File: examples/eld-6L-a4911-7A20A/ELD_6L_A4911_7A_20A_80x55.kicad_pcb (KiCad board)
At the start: 6 copper layers, 80 x 55 mm, 103 parts, among them J1 BAT/IGN/GND, J2 DAP, J3 CAN, J4 ELD, J5 UART, Q1 SQD50P04-09L, Q2 IAUC60N04S6N050H, Q3 IAUC60N04S6N050H, U1 TPS54331, U2 AMS1117-3.3, U3 TC364DP, U4 TPS3823-33, U5 TLE9251V, U6 A4911, Y1 20MHz

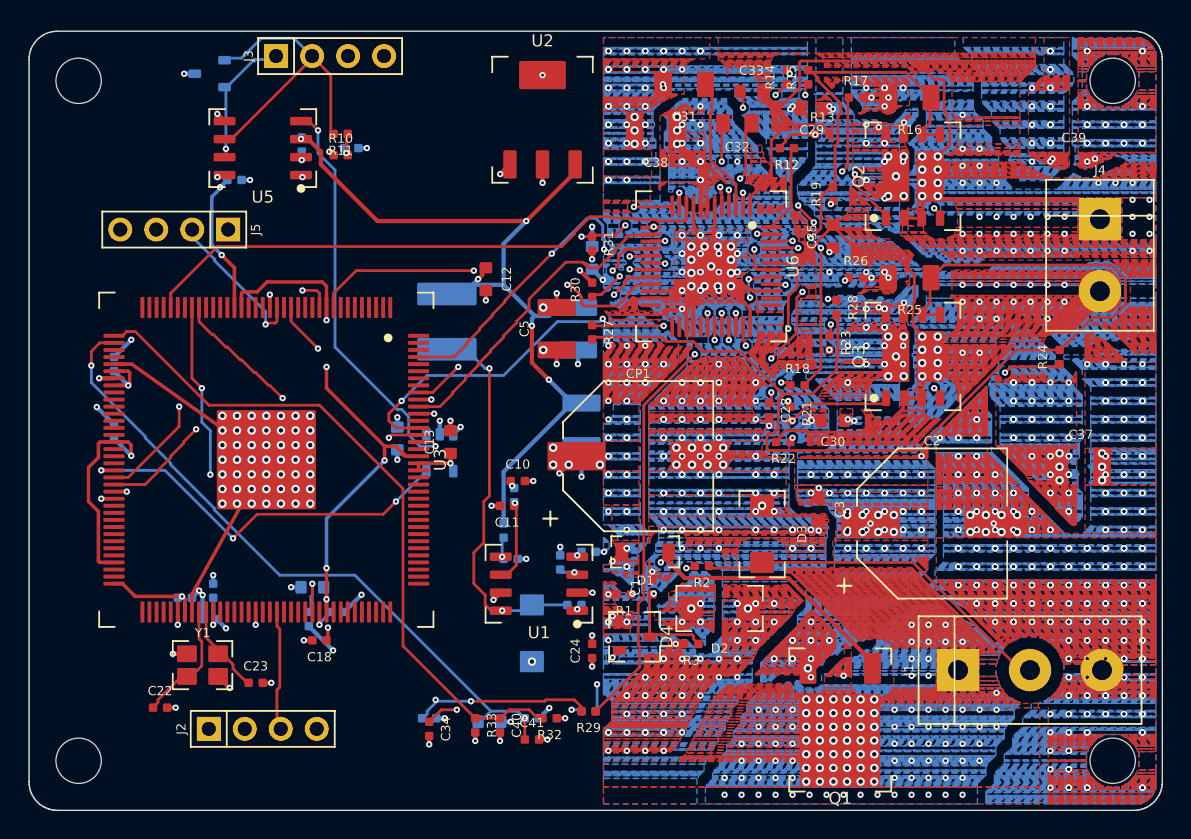
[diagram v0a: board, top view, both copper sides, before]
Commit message: v1.83.0 one ECU connector: Molex MX150 sealed right-angle header for ELD only
- pwr_in conn=ecu folds the supply, IGN, load output and CAN connectors into one MX150 2-row header; parallel contacts per
  power signal (15 A max per contact: 20 A peak -> 2), column-wise pin map, standard sizes 4-20
- ELD only default: MX150 2x6 (BAT x2, GND x2, ELD+ x2, ELD- x2, IGN, CAN_H, CAN_L, NC); footprint dims assumed
- power macro: ECU-connector layout (connector on the zone's bottom edge, body to the board edge, bridge column above the
  load contacts, supply FET over the BAT column, driver beside the column if free)
- example eld6 regenerated: 6 layers 80 x 55, 0 unrouted, DRC 0, power widths / vias / planes pass

Co-Authored-By: Claude Opus 5.5 <noreply@anthropic.com>
Claude-Session: https://claude.ai/code/session_01ENBZQtx2ruaEBZiZmBjLaq
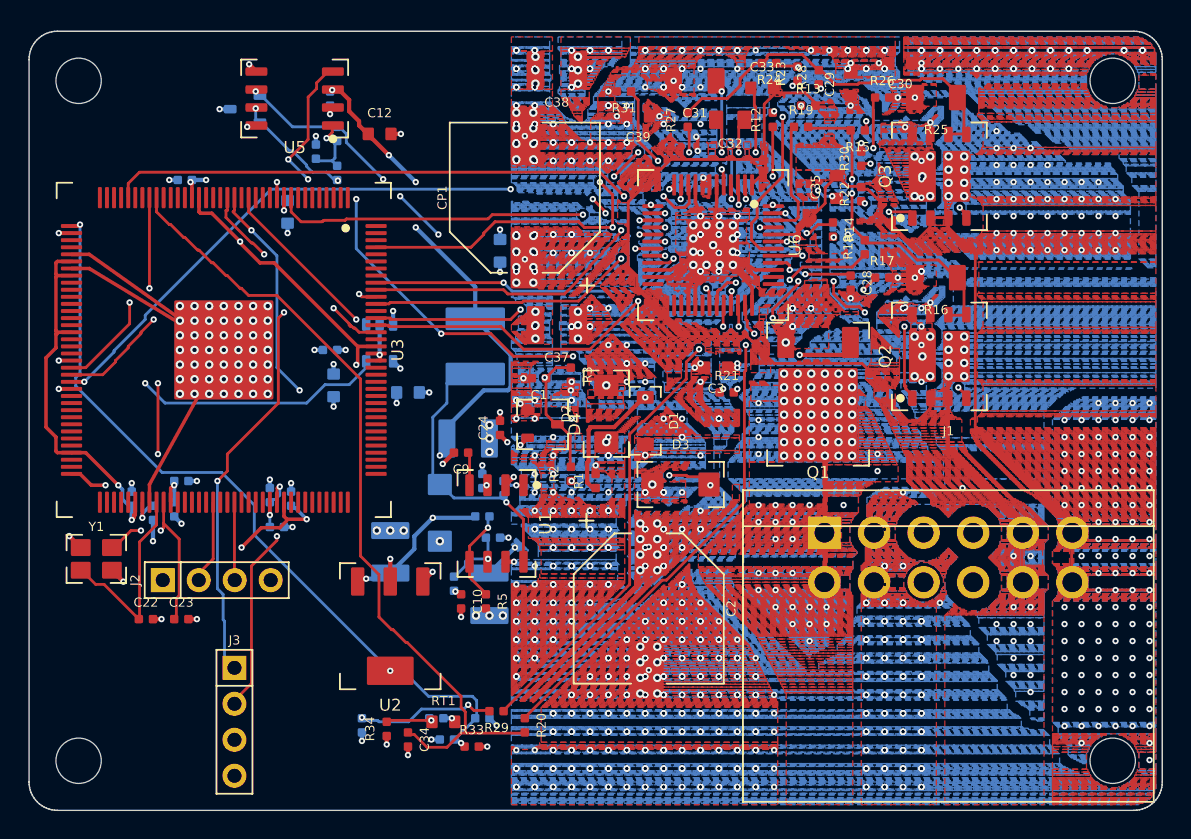
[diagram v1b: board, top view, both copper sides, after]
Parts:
- removed J4: ELD, pcb_viewer:TERM-2-5.08
- removed J5: UART, pcb_viewer:HDR-1x4
- C11, C13, C18, C40, C41, C5, R10, R11, R32: moved to B.Cu
- C9, R20, R34, R5, RT1: moved to F.Cu
- J1: value BAT/IGN/GND -> ECU; footprint pcb_viewer:TERM-3-5.08 -> pcb_viewer:MX150-2x6-RA
- J3: value CAN -> UART
- moved J3 47.5 mm to (39.5, 73.8), turned to 0 degrees
- moved C37 38.3 mm to (62.2, 45.8), turned to 180 degrees
- moved U2 37.3 mm to (50.5, 67.0), turned to 180 degrees
- moved C39 30.9 mm to (68.0, 31.0), turned to 180 degrees
- moved R24 29.2 mm to (77.2, 27.2), turned to 180 degrees
- moved C20 26.6 mm to (43.2, 37.8), turned to 90 degrees
- moved C30 25.7 mm to (86.5, 27.2)
- moved Q1 23.1 mm to (80.7, 51.5)
- moved R30 21.1 mm to (83.8, 34.0)
- moved C2 20.9 mm to (68.8, 65.8), turned to 270 degrees
- moved R3 20.8 mm to (63.2, 49.2), turned to 270 degrees
- moved C7 20.6 mm to (50.5, 61.8), turned to 270 degrees
- moved CP1 19.9 mm to (60.0, 36.8), turned to 90 degrees
- moved C5 19.3 mm to (57.5, 64.8)
- moved R23 19.1 mm to (79.2, 28.0), turned to 90 degrees
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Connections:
- J1 pad 2: IGN_IN -> GND
- J1 pad 3: GND -> IGN_IN
- J3 pad 1: CANH -> DBG_TX
- J3 pad 2: CANL -> DBG_RX
- J3 pad 4: (no net) -> +3V3
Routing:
- net HB_B_SNS: track 78.2 -> 26.9 mm
- net CANH: track 18.1 -> 66.3 mm, vias 2 -> 5
- net CANL: track 22.1 -> 66.4 mm, vias 0 -> 4
- net HB_A_HG: track 11.0 -> 42.6 mm, vias 2 -> 3
- net DBG_TX: track 6.73 -> 37.5 mm, vias 1 -> 3
- net DBG_RX: track 10.7 -> 39.6 mm, vias 1 -> 3
- net HB_A: track 53.2 -> 73.7 mm, vias 47 -> 24
- net HB_DIAG: track 28.4 -> 48.7 mm, vias 4 -> 6
- net HB_A_LG: track 17.0 -> 34.5 mm, vias 3 -> 5
- net HB_A_SNS: track 38.1 -> 23.0 mm
- net HB_B_HG: track 9.04 -> 23.1 mm, vias 2 -> 3
- net IGN_DET: track 47.6 -> 36.0 mm, vias 3 -> 2
- net +5V: track 60.0 -> 49.6 mm, vias 5 -> 7
- net HB_B_LSS: track 9.24 -> 19.4 mm, vias 3 -> 2
- net HB_EN: track 49.6 -> 58.6 mm, vias 4 -> 3
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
